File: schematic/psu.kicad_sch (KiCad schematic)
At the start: 9 parts, among them J10 Conn_01x02, J11 Conn_01x02, SW1 SW_Push, SW2 SW_SPDT

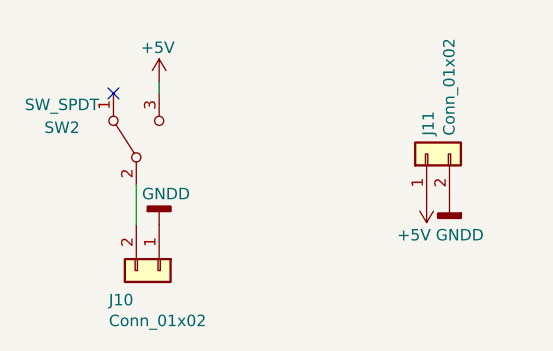
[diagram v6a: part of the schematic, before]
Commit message: updated output jacks to correct footprint
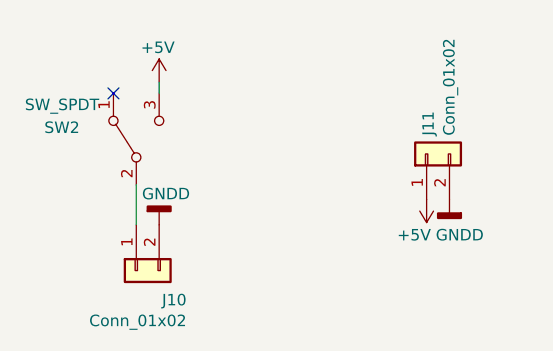
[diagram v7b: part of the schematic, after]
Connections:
- net GNDD: now also J10.2 (Pin_2); no longer J10.1 (Pin_1)
- net at SW2.2 (B): now also J10.1 (Pin_1); no longer J10.2 (Pin_2)
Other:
- moved on the sheet: J10
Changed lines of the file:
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@@
     )
   )
-  (symbol (lib_id "Connector_Generic:Conn_01x02") (at 92.837 107.188 270) (unit 1)
+  (symbol (lib_id "Connector_Generic:Conn_01x02") (at 90.297 107.188 90) (mirror x) (unit 1)
     (in_bom yes) (on_board yes) (dnp no)
-    (property "Reference" "J10" (at 87.249 110.4646 90)
+    (property "Reference" "J10" (at 95.885 110.4646 90)
       (effects (font (size 1.27 1.27)) (justify left))
     )
-    (property "Value" "Conn_01x02" (at 87.249 112.776 90)
+    (property "Value" "Conn_01x02" (at 95.885 112.776 90)
       (effects (font (size 1.27 1.27)) (justify left))
     )
-    (property "Footprint" "Connector_Molex:Molex_KK-254_AE-6410-02A_1x02_P2.54mm_Vertical" (at 92.837 107.188 0)
+    (property "Footprint" "Connector_Molex:Molex_KK-254_AE-6410-02A_1x02_P2.54mm_Vertical" (at 90.297 107.188 0)
       (effects (font (size 1.27 1.27)) hide)
     )
-    (property "Datasheet" "~" (at 92.837 107.188 0)
+    (property "Datasheet" "~" (at 90.297 107.188 0)
       (effects (font (size 1.27 1.27)) hide)
     )
